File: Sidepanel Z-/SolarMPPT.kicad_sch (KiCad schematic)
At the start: 46 parts, among them U11 INA180A4, U12 INA180A4

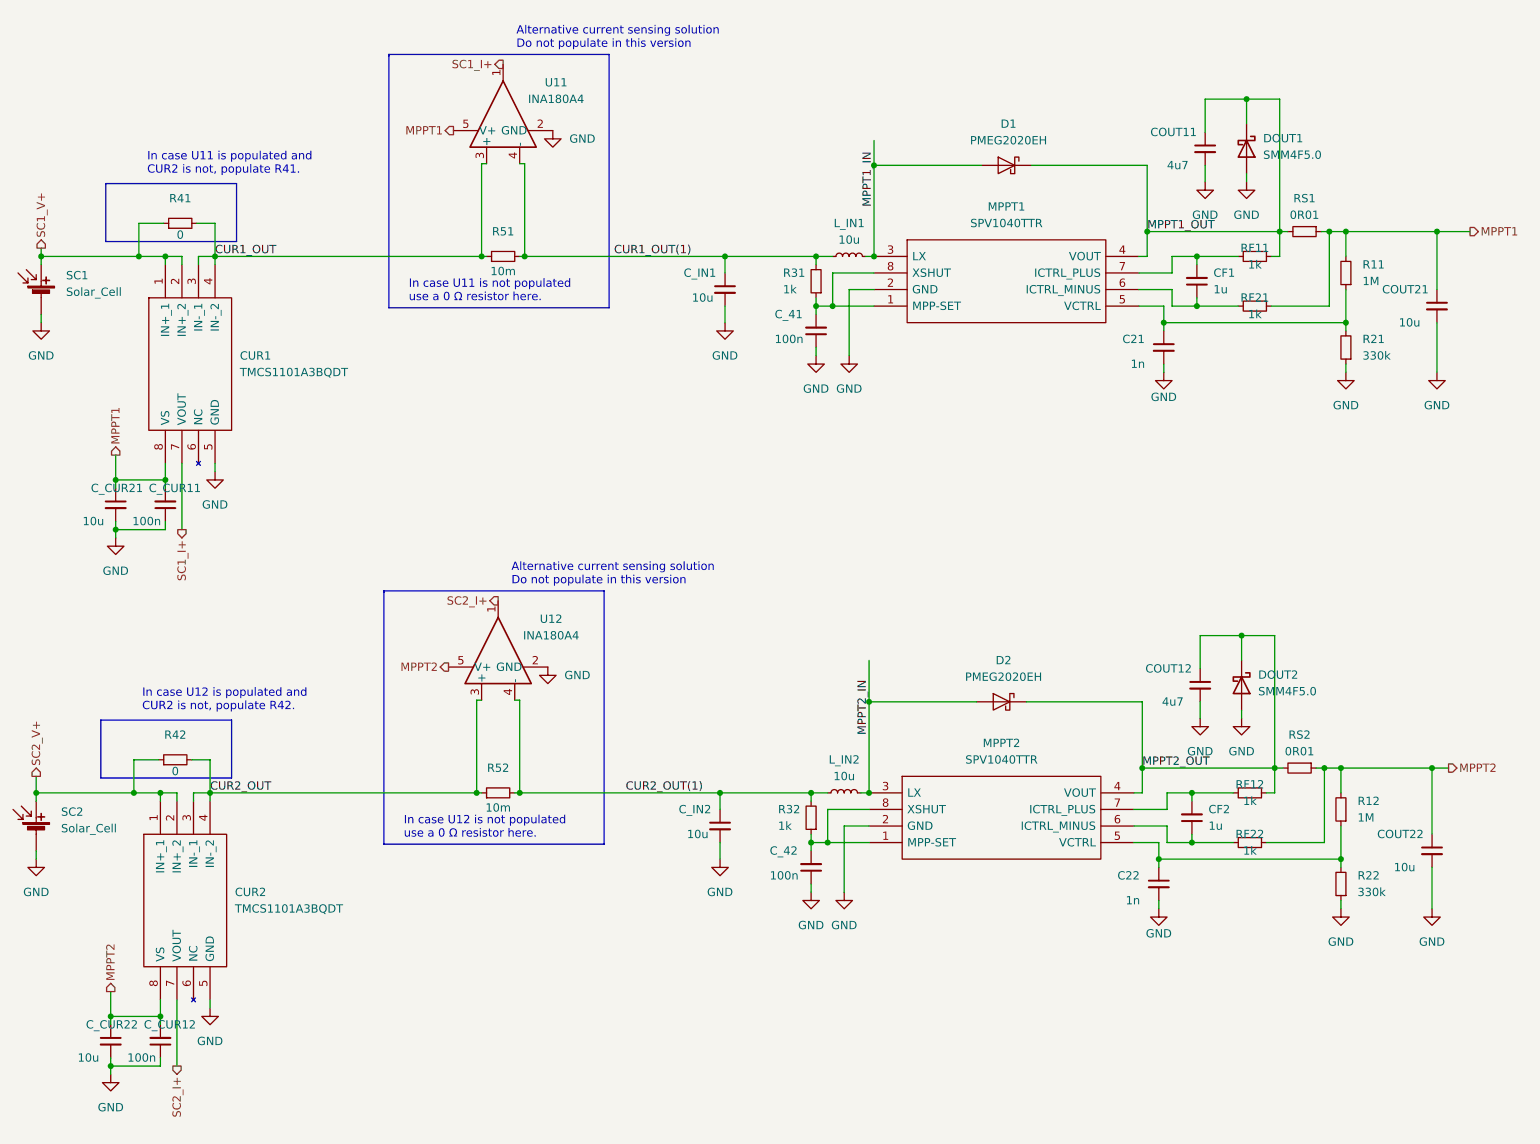
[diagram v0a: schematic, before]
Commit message: Changed the layout of all the sidepanel PCBs to mitigate the problems that arised from the bad previous design.
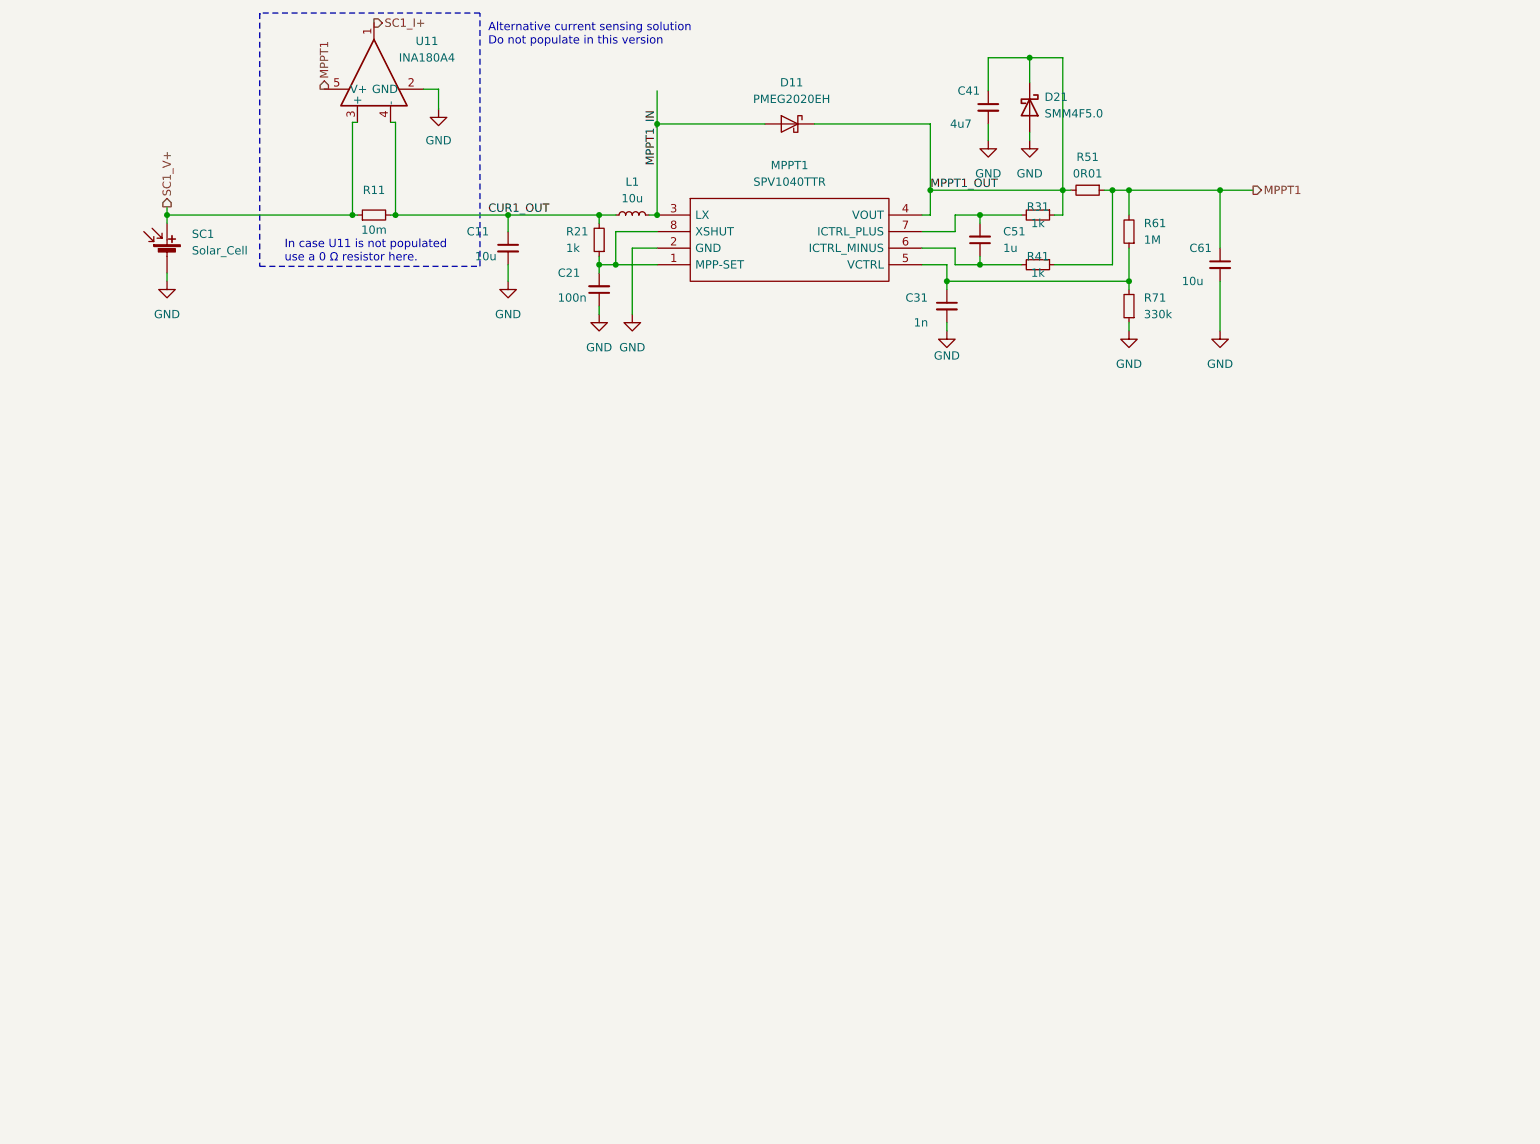
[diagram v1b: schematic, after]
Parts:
- removed C22: 1n, Capacitor_SMD:C_0603_1608Metric, symbol Device:C_Small
- removed CF2: 1u, Capacitor_SMD:C_0603_1608Metric, symbol Device:C_Small
- removed COUT12: 4u7, Capacitor_SMD:C_0603_1608Metric, symbol Device:C_Small
- removed COUT22, C_CUR21, C_CUR22, C_IN2: 10u, Capacitor_SMD:C_0603_1608Metric, symbol Device:C_Small
- removed CUR1, CUR2: TMCS1101A3BQDT, Package_SO:SOIC-8_3.9x4.9mm_P1.27mm, symbol SamacSys_Parts:TMCS1101A3BQDT
- removed C_42, C_CUR11, C_CUR12: 100n, Capacitor_SMD:C_0603_1608Metric, symbol Device:C_Small
- removed D1, D2: PMEG2020EH, Diode_SMD:D_SOD-123F, symbol Diode:PMEG2020EH
- removed DOUT2: SMM4F5.0, SamacSys:STMITE, symbol Device:D_Schottky
- removed L_IN2: 10u, STS_Inductor_SMD:XAL6060103MEC, symbol Device:L_Small
- removed MPPT2: SPV1040TTR, Package_SO:TSSOP-8_4.4x3mm_P0.65mm, symbol SamacSys:SPV1040TTR
- removed R12: 1M, Resistor_SMD:R_0603_1608Metric, symbol Device:R_Small
- removed R22: 330k, Resistor_SMD:R_0603_1608Metric, symbol Device:R_Small
- removed R32, RF12, RF22: 1k, Resistor_SMD:R_0603_1608Metric, symbol Device:R_Small
- removed R41, R42: 0, Resistor_SMD:R_0603_1608Metric, symbol Device:R_Small
- removed R51, R52: 10m, Resistor_SMD:R_0603_1608Metric, symbol Device:R_Small
- removed RS2: 0R01, Resistor_SMD:R_0603_1608Metric, symbol Device:R_Small
- removed SC2: Solar_Cell, STS_solder:3G30A_40x80_Z_SC2, symbol Device:Solar_Cell
- removed U12: INA180A4, Package_TO_SOT_SMD:SOT-23-5, symbol Amplifier_Current:INA180A4
- added D11: PMEG2020EH, Diode_SMD:D_SOD-123F, symbol Diode:PMEG2020EH
- added R11: 10m, Resistor_SMD:R_0603_1608Metric, symbol Device:R_Small
- D21: renamed from DOUT1; footprint SamacSys:STMITE -> STS_semiconductor:DIO_SMM4F5.0A-TR
- L1: renamed from L_IN1; footprint STS_Inductor_SMD:XAL6060103MEC -> STS_Inductor_SMD:IND_XAL6060-103MEC
- SC1: footprint STS_solder:3G30A_40x80_Z_SC1 -> STS_solder:3G30A_40x80
- renumbered C_IN1 to C11, C_41 to C21, C21 to C31, COUT11 to C41, CF1 to C51, COUT21 to C61, R31 to R21, RF11 to R31, RF21 to R41, RS1 to R51, R11 to R61, R21 to R71
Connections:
- net CUR1_OUT(1) is gone; now on net CUR1_OUT: C11.1, L1.1, R21.2, U11.4 (-)
- net CUR1_OUT: now also R11.2; no longer U11.3 (+)
- net MPPT1_IN: now also D11.2 (A)
- net MPPT1_OUT: now also D11.1 (K)
- net SC1_V+: now also U11.3 (+), R11.1
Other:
- note removed: "In case U11 is populated and CUR2 is not, populate R41."
- note removed: "In case U12 is not populated use a 0 Ω resistor here."
- note removed: "In case U12 is populated and CUR2 is not, populate R42."
- moved on the sheet: C11, C21, C31, C41, C51, C61, D21, L1, MPPT1, R21, R31, R41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

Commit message: moved the connectors, changed the footprint of the input and output capacitors and splitted the input capacitor in two
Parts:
- C11, C61: value 10u -> 22u; footprint Capacitor_SMD:C_0603_1608Metric -> Capacitor_SMD:C_0805_2012Metric
- C41: value 4u7 -> 22u; footprint Capacitor_SMD:C_0603_1608Metric -> Capacitor_SMD:C_0805_2012Metric
- R11: footprint Resistor_SMD:R_0603_1608Metric -> Resistor_SMD:R_0805_2012Metric
- R51: value 0R01 -> 220m; footprint Resistor_SMD:R_0603_1608Metric -> Resistor_SMD:R_0805_2012Metric
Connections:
- net CUR1_OUT: now also C61.1
- net MPPT1: no longer C61.1
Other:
- note removed: "Alternative current sensing solution Do not populate in this version"
- note removed: "In case U11 is not populated use a 0 Ω resistor here."
- moved on the sheet: C11

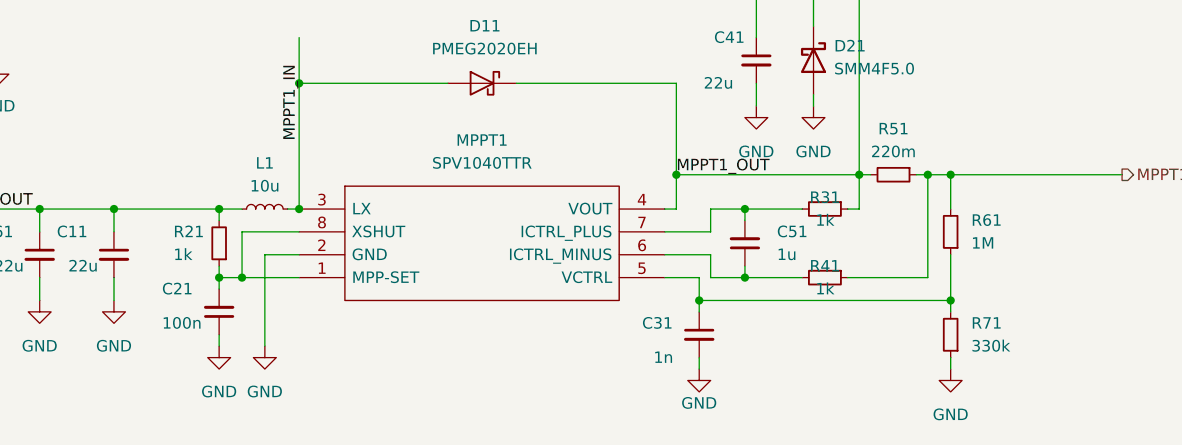
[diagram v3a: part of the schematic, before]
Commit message: Changed the values of the VCTRL resistors.
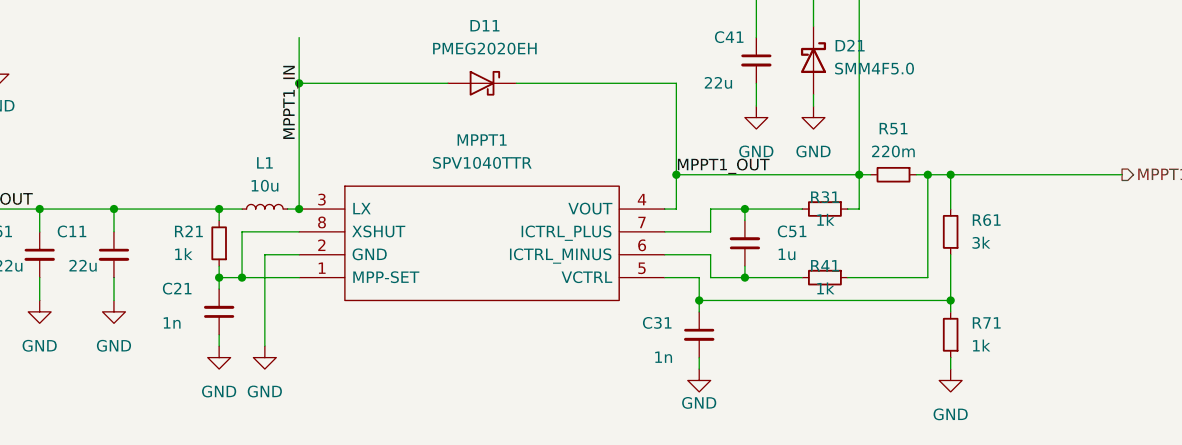
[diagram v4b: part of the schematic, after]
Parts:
- C21: value 100n -> 1n
- R61: value 1M -> 3k
- R71: value 330k -> 1k
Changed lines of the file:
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@@
 		(fields_autoplaced yes)
 		(property "Reference" "R71"
-			(at 207.01 59.69 0)
-			(effects
-				(font
-					(size 1.27 1.27)
-				)
-				(justify right)
-			)
-		)
-		(property "Value" "330k"
-			(at 207.01 62.23 0)
+			(at 207.01 59.6899 0)
+			(effects
+				(font
+					(size 1.27 1.27)
+				)
+				(justify right)
+			)
+		)
+		(property "Value" "1k"
+			(at 207.01 62.2299 0)
 			(effects
 				(font
@@
 		(fields_autoplaced yes)
 		(property "Reference" "R61"
-			(at 207.01 48.26 0)
-			(effects
-				(font
-					(size 1.27 1.27)
-				)
-				(justify right)
-			)
-		)
-		(property "Value" "1M"
-			(at 207.01 50.8 0)
+			(at 207.01 48.2599 0)
+			(effects
+				(font
+					(size 1.27 1.27)
+				)
+				(justify right)
+			)
+		)
+		(property "Value" "3k"
+			(at 207.01 50.7999 0)
 			(effects
 				(font
@@
 			)
 		)
-		(property "Value" "100n"
+		(property "Value" "1n"
 			(at 117.094 59.69 0)
 			(effects

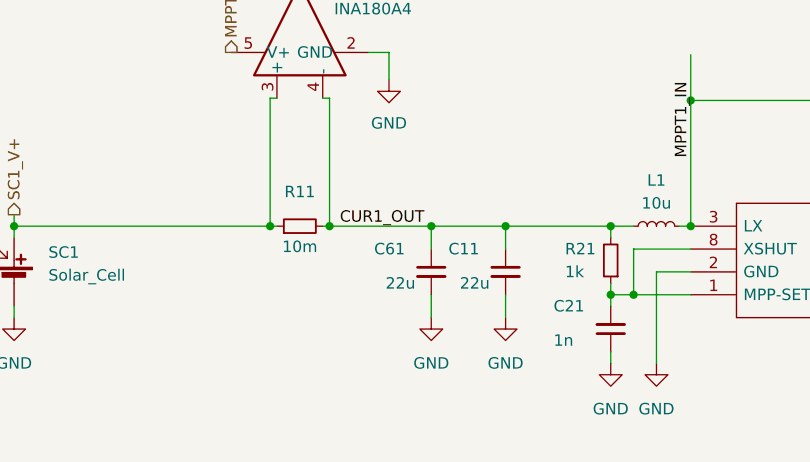
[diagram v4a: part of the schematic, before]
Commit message: Changed one of the inputs capacitors for all panels with one of 1 uF and lower ESR and moved some traces that were under the inductor.
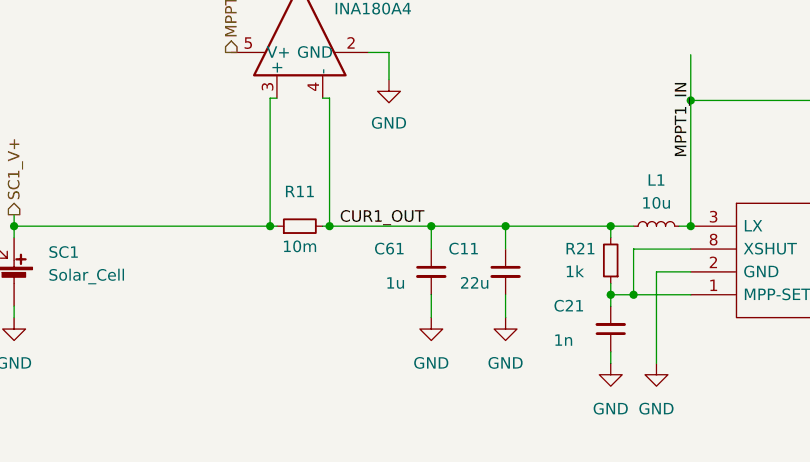
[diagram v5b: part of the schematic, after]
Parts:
- C61: value 22u -> 1u
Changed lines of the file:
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@@
 			)
 		)
-		(property "Value" "22u"
+		(property "Value" "1u"
 			(at 98.425 53.34 0)
 			(effects
@@
 			)
 		)
-		(property "Description" ""
+		(property "Description" "TMK212B7105KGHTR"
 			(at 103.505 52.07 0)
 			(effects
